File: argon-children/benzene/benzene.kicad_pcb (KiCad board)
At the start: 2 copper layers, 0 parts

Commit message: Benzene footprints
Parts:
- added C1: 100nF, Capacitor_SMD:C_0603_1608Metric, F.Cu at (96.2, 62.6)
- added C2: 10uF, Capacitor_SMD:C_0603_1608Metric, F.Cu at (116.4, 50.8)
- added C3: 10uF, Capacitor_SMD:C_0603_1608Metric, F.Cu at (100.2, 62.6)
- added C4: 1uF, Capacitor_SMD:C_0603_1608Metric, F.Cu at (104.2, 64.4)
- added D1: LED, LED_SMD:LED_0805_2012Metric, F.Cu at (91.7, 63.3)
- added R1: 47R, Resistor_SMD:R_0603_1608Metric, F.Cu at (116.4, 53.3)
- added R2: 47R, Resistor_SMD:R_0603_1608Metric, F.Cu at (112.6, 57.2)
- added R3: 47R, Resistor_SMD:R_0603_1608Metric, F.Cu at (108.2, 64.4)
- added R4: 47R, Resistor_SMD:R_0603_1608Metric, F.Cu at (112.6, 59.7)
- added R5: 1.5K, Resistor_SMD:R_0603_1608Metric, F.Cu at (116.6, 55.8)
- added R6: 330R, Resistor_SMD:R_0603_1608Metric, F.Cu at (116.6, 58.3)
- added R7: 100K, Resistor_SMD:R_0603_1608Metric, F.Cu at (112.6, 62.2)
- added U1: Conn1, Connector_PinHeader_2.54mm:PinHeader_1x02_P2.54mm_Vertical, F.Cu at (108.2, 58.3)
- added U2: SPI FLASH, Package_DIP:DIP-8_W7.62mm_Socket, F.Cu at (96.2, 40.0)
- added U3: Conn2, Connector_PinHeader_2.54mm:PinHeader_1x04_P2.54mm_Vertical, F.Cu at (91.8, 51.8)
- added U4: LMC555, Package_SO:SOIC-8_3.9x4.9mm_P1.27mm, F.Cu at (110.1, 52.7)

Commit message: Benzene - PCB, part 1
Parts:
- C3, R5, R6, U1, U3: moved to B.Cu
- U4: footprint Package_SO:SOIC-8_3.9x4.9mm_P1.27mm -> Package_SO:VSSOP-8_3.0x3.0mm_P0.65mm; moved to B.Cu
- moved C2 34.8 mm to (96.0, 78.9), turned to 180 degrees
- moved U2 34.0 mm to (99.3, 73.8)
- moved R1 30.8 mm to (96.0, 76.4)
- moved R5 30.7 mm to (96.5, 79.0)
- moved U3 29.7 mm to (93.0, 81.5)
- moved U4 25.8 mm to (103.1, 77.6), turned to 270 degrees
- moved R2 23.5 mm to (96.0, 73.8)
- moved R4 19.3 mm to (110.3, 78.9), turned to 180 degrees
- moved R6 19.3 mm to (103.1, 72.1), turned to 180 degrees
- moved C3 19.0 mm to (109.7, 79.0)
- moved U1 18.9 mm to (113.3, 76.5), turned to 180 degrees
- moved C1 18.8 mm to (96.0, 81.5), turned to 180 degrees
- moved R3 17.2 mm to (110.3, 81.5)
- moved C4 13.4 mm to (110.2, 76.4)
- moved D1 13.4 mm to (103.1, 70.3), turned to 180 degrees
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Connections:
- R1 pad 2: ~CS -> Net-(R1-Pad2)
- R2 pad 2: Net-(R2-Pad2) -> ~CS
- U3 pad 3: Net-(R2-Pad2) -> ~CS
- U3 pad 4: ~CS -> Net-(R1-Pad2)
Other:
- board outline added: 30.5 x 16.3 mm
- net class Default: clearance 0.2 -> 0.127; trace_width 0.25 -> 0.127
- net class zasilanie added: clearance 0.381, trace_width 0.381, via_dia 1.143, via_drill 0.508
- rule trace_clearance: 0.2 -> 0.127
- rule trace_min: 0.2 -> 0.1
- board text added: "3V3"
- board text added: "CLK"
- board text added: "CS"
- board text added: "GND"
- board text added: "MISO"
- board text added: "MOSI"

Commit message: Benzene - part 2 PCB
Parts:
- turned R3 to 180 degrees
- turned R1 to 180 degrees
- turned R2 to 180 degrees
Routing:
- net V3V3: track 0.00 -> 42.3 mm
- net Net-(R3-Pad2): track 0.00 -> 25.0 mm, vias 0 -> 1
- net Net-(R4-Pad2): track 0.00 -> 24.9 mm, vias 0 -> 1
- net ~CS: track 0.00 -> 24.1 mm, vias 0 -> 1
- net GND: track 0.00 -> 23.1 mm, vias 0 -> 5
- net Net-(C4-Pad1): track 0.00 -> 11.8 mm, vias 0 -> 1
- net Net-(C3-Pad1): track 0.00 -> 5.54 mm
- net Net-(R3-Pad1): track 0.00 -> 5.10 mm
- net Net-(R4-Pad1): track 0.00 -> 5.10 mm
- net Net-(R1-Pad2): track 0.00 -> 3.47 mm
- net Net-(R6-Pad1): track 0.00 -> 3.46 mm
- net Net-(D1-Pad2): track 0.00 -> 3.30 mm, vias 0 -> 1
- net Net-(R2-Pad1): track 0.00 -> 2.54 mm
- net Net-(R1-Pad1): track 0.00 -> 2.54 mm
- added copper zone on B.Cu, net GND

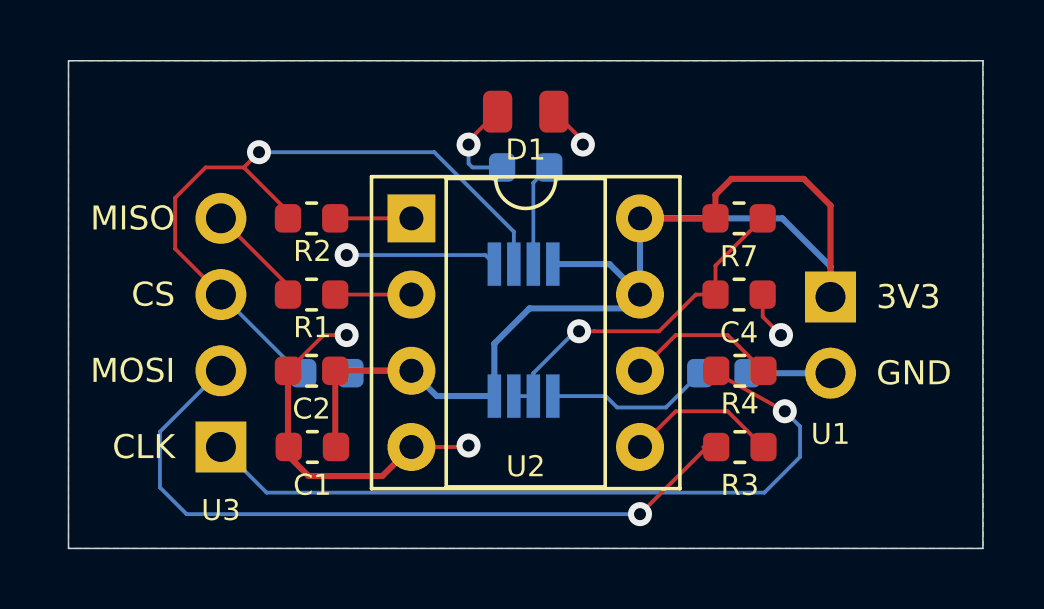
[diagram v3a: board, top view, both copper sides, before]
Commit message: Benzene - verson with logo and centered 2 pins
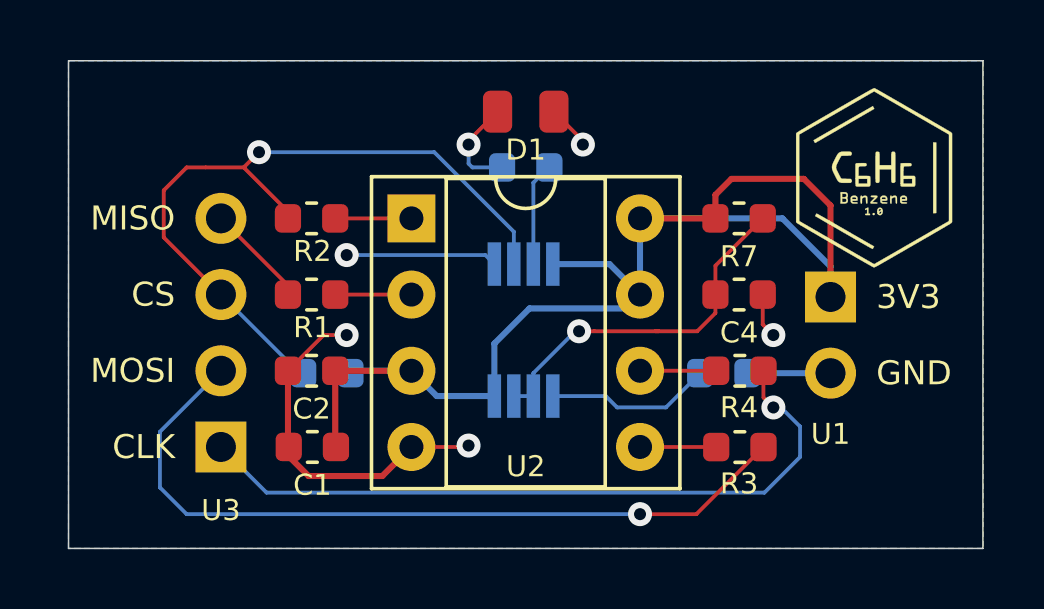
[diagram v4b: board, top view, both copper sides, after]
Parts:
- added G***: LOGO, benzene:benzene-logo2, F.Cu at (114.7, 72.5)
- turned R3 to 0 degrees
- turned R4 to 0 degrees
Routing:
- net Net-(R4-Pad1): track 5.10 -> 2.62 mm
- net Net-(R3-Pad1): track 5.10 -> 2.85 mm
- net Net-(R4-Pad2): track 24.9 -> 23.5 mm
- net Net-(R3-Pad2): track 25.0 -> 26.1 mm
- net ~CS: track 24.1 -> 24.8 mm

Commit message: Add logos & author
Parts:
- removed the G*** at (114.7, 72.5)
- added G***: LOGO, benzene:type, F.Cu at (90.9, 70.1)
- added G***: LOGO, benzene:author, B.Cu at (115.1, 71.2)
- added G***: LOGO, benzene:logo-wlasciwe, F.Cu at (114.9, 72.5)
- moved U1 2.54 mm to (113.3, 79.0)
- turned R7 to 180 degrees
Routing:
- net V3V3: track 42.3 -> 34.6 mm
- net GND: track 23.0 -> 20.2 mm
- net Net-(C4-Pad1): track 12.2 -> 11.6 mm

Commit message: Benzene prealpha
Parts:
- moved G*** 0.51 mm to (90.4, 70.1)
- moved G*** 0.38 mm to (115.5, 71.2)
- moved G*** 0.36 mm to (115.1, 72.7)
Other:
- board size 30.5 x 16.3 mm -> 31.5 x 16.3 mm
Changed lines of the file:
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@@
   (general
     (thickness 1.6)
-    (drawings 10)
+    (drawings 12)
     (tracks 108)
     (zones 0)
@@
   )
   (layers
-    (0 F.Cu signal hide)
-    (31 B.Cu signal hide)
+    (0 F.Cu signal)
+    (31 B.Cu signal)
     (32 B.Adhes user hide)
     (33 F.Adhes user hide)
@@
     (38 B.Mask user hide)
     (39 F.Mask user hide)
-    (40 Dwgs.User user hide)
+    (40 Dwgs.User user)
     (41 Cmts.User user hide)
     (42 Eco1.User user hide)
@@
   )
   (module benzene:type (layer F.Cu)
-    (at 90.861 70.06499)
+    (at 90.353 70.06499)
     (fp_text reference G*** (at 0 0) (layer F.SilkS) hide
       (effects (font (size 1.524 1.524) (thickness 0.3)))
@@
   )
   (module benzene:author (layer B.Cu)
-    (at 115.118 71.20799 180)
+    (at 115.499 71.20799 180)
     (fp_text reference G*** (at 0 0) (layer B.SilkS) hide
       (effects (font (size 1.524 1.524) (thickness 0.3)) (justify mirror))
@@
   )
   (module benzene:logo-wlasciwe (layer F.Cu)
-    (at 114.864 72.47799)
+    (at 115.118 72.73199)
     (fp_text reference G*** (at 0 0) (layer F.SilkS) hide
       (effects (font (size 1.524 1.524) (thickness 0.3)))
     )
-    (fp_text value LOGO (at 0.75 0) (layer F.SilkS) hide
+    (fp_text value LOGO (at 1.016 0) (layer F.SilkS) hide
       (effects (font (size 1.524 1.524) (thickness 0.3)))
     )
@@
     )
   )
-  (gr_line (start 118.364 68.58) (end 87.884 68.58) (layer Edge.Cuts) (width 0.05))
-  (gr_line (start 118.364 84.836) (end 118.364 68.58) (layer Edge.Cuts) (width 0.05))
-  (gr_line (start 87.884 84.836) (end 118.364 84.836) (layer Edge.Cuts) (width 0.05))
-  (gr_line (start 87.884 68.58) (end 87.884 84.836) (layer Edge.Cuts) (width 0.05))
+  (dimension 31.48 (width 0.15) (layer Dwgs.User)
+    (gr_text "31.480 mm" (at 103.124 89.01799) (layer Dwgs.User)
+      (effects (font (size 1 1) (thickness 0.15)))
+    )
+    (feature1 (pts (xy 118.864 84.836) (xy 118.864 88.304411)))
+    (feature2 (pts (xy 87.384 84.836) (xy 87.384 88.304411)))
+    (crossbar (pts (xy 87.384 87.71799) (xy 118.864 87.71799)))
+    (arrow1a (pts (xy 118.864 87.71799) (xy 117.737496 88.304411)))
+    (arrow1b (pts (xy 118.864 87.71799) (xy 117.737496 87.131569)))
+    (arrow2a (pts (xy 87.384 87.71799) (xy 88.510504 88.304411)))
+    (arrow2b (pts (xy 87.384 87.71799) (xy 88.510504 87.131569)))
+  )
+  (dimension 16.256 (width 0.15) (layer Dwgs.User)
+    (gr_text "16.256 mm" (at 125.435 76.708 90) (layer Dwgs.User)
+      (effects (font (size 1 1) (thickness 0.15)))
+    )
+    (feature1 (pts (xy 118.864 68.58) (xy 124.721421 68.58)))
+    (feature2 (pts (xy 118.864 84.836) (xy 124.721421 84.836)))
+    (crossbar (pts (xy 124.135 84.836) (xy 124.135 68.58)))
+    (arrow1a (pts (xy 124.135 68.58) (xy 124.721421 69.706504)))
+    (arrow1b (pts (xy 124.135 68.58) (xy 123.548579 69.706504)))
+    (arrow2a (pts (xy 124.135 84.836) (xy 124.721421 83.709496)))
+    (arrow2b (pts (xy 124.135 84.836) (xy 123.548579 83.709496)))
+  )
+  (gr_line (start 118.864 68.58) (end 87.384 68.58) (layer Edge.Cuts) (width 0.05))
+  (gr_line (start 118.864 84.836) (end 118.864 68.58) (layer Edge.Cuts) (width 0.05))
+  (gr_line (start 87.384 84.836) (end 118.864 84.836) (layer Edge.Cuts) (width 0.05))
+  (gr_line (start 87.384 68.58) (end 87.384 84.836) (layer Edge.Cuts) (width 0.05))
   (gr_text 3V3 (at 114.808 78.994) (layer F.SilkS)
     (effects (font (size 0.8 0.8) (thickness 0.15)) (justify left))

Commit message: 25x15 - part1
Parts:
- C1, C2, C4, R1, R2, R3, R4, R7: moved to B.Cu
- moved R1 6.26 mm to (97.0, 70.2)
- moved C4 6.18 mm to (110.2, 70.2)
- moved C3 3.71 mm to (110.2, 75.3)
- moved R5 3.66 mm to (97.0, 75.4)
- moved G*** 3.61 mm to (93.9, 69.4)
- moved U3 3.21 mm to (96.0, 80.4)
- moved G*** 2.71 mm to (112.5, 72.2)
- moved U1 2.27 mm to (111.3, 78.0)
- moved G*** 2.27 mm to (113.5, 70.2)
- moved R2 1.45 mm to (97.0, 72.8)
- moved C1 1.44 mm to (97.0, 80.4)
- moved C2 1.41 mm to (97.0, 77.9)
- moved D1 1.14 mm to (103.6, 69.3)
- moved U2 1.14 mm to (99.8, 72.8)
- moved U4 1.14 mm to (103.6, 76.5)
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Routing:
- net Net-(R3-Pad2): track 26.1 -> 0.00 mm, vias 1 -> 0
- net ~CS: track 24.8 -> 0.00 mm, vias 1 -> 0
- net Net-(R4-Pad2): track 23.5 -> 0.00 mm, vias 1 -> 0
- net GND: track 20.2 -> 1.56 mm, vias 5 -> 1
- net V3V3: track 34.6 -> 16.6 mm
- net Net-(C4-Pad1): track 11.6 -> 1.41 mm, vias 1 -> 0
- net Net-(R1-Pad2): track 3.47 -> 0.00 mm
- net Net-(R3-Pad1): track 2.85 -> 0.00 mm
- net Net-(R4-Pad1): track 2.62 -> 0.00 mm
- net Net-(R2-Pad1): track 2.54 -> 0.00 mm
- net Net-(R1-Pad1): track 2.54 -> 0.00 mm
- removed copper zone on B.Cu, net GND
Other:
- board size 31.5 x 16.3 mm -> 25 x 15 mm

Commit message: Benzene refactored
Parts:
- R3, R4: moved to F.Cu
- U2: footprint Package_DIP:DIP-8_W7.62mm_Socket -> benzene:DIP-8_W7.62mm_Socket
- moved R7 18.6 mm to (93.1, 80.1), turned to 270 degrees
- moved C2 17.8 mm to (114.3, 73.9), turned to 270 degrees
- moved C1 16.8 mm to (112.5, 73.9), turned to 270 degrees
- moved C4 10.7 mm to (114.3, 80.1), turned to 90 degrees
- moved R3 7.73 mm to (103.6, 76.5), turned to 180 degrees
- moved R4 6.78 mm to (103.6, 79.1), turned to 180 degrees
- moved R2 4.37 mm to (93.1, 71.0), turned to 270 degrees
- moved R5 3.95 mm to (93.1, 75.4), turned to 270 degrees
- moved C3 1.54 mm to (109.7, 73.9), turned to 90 degrees
- moved R1 1.15 mm to (96.0, 69.7)
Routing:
- net Net-(C4-Pad1): track 1.41 -> 29.2 mm
- net GND: track 1.56 -> 28.8 mm, vias 1 -> 2
- net V3V3: track 16.6 -> 42.0 mm
- net ~CS: track 0.00 -> 17.2 mm
- net Net-(R2-Pad1): track 0.00 -> 10.6 mm
- net Net-(R3-Pad1): track 0.00 -> 8.93 mm
- net Net-(C3-Pad1): track 5.54 -> 14.2 mm
- net Net-(R4-Pad2): track 0.00 -> 7.35 mm
- net Net-(R3-Pad2): track 0.00 -> 7.35 mm
- net Net-(R1-Pad1): track 0.00 -> 6.94 mm
- net Net-(R4-Pad1): track 0.00 -> 3.56 mm
- net Net-(R1-Pad2): track 0.00 -> 3.48 mm
- added copper zone on F.Cu, net GND
